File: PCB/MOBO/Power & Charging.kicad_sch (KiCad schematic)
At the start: 53 parts, among them J201 USB_C_Receptacle_PowerOnly_6P, Q1 Si4435DDY, Q2 IRLML6344, Q4 AO3401A, Q5 FS8205A, SW1 SW_DPST_x2, U1 LC709203FQH-01TWG, U2 DW01A, U202 MCP73871-1AA, U205 TPS61230DRC

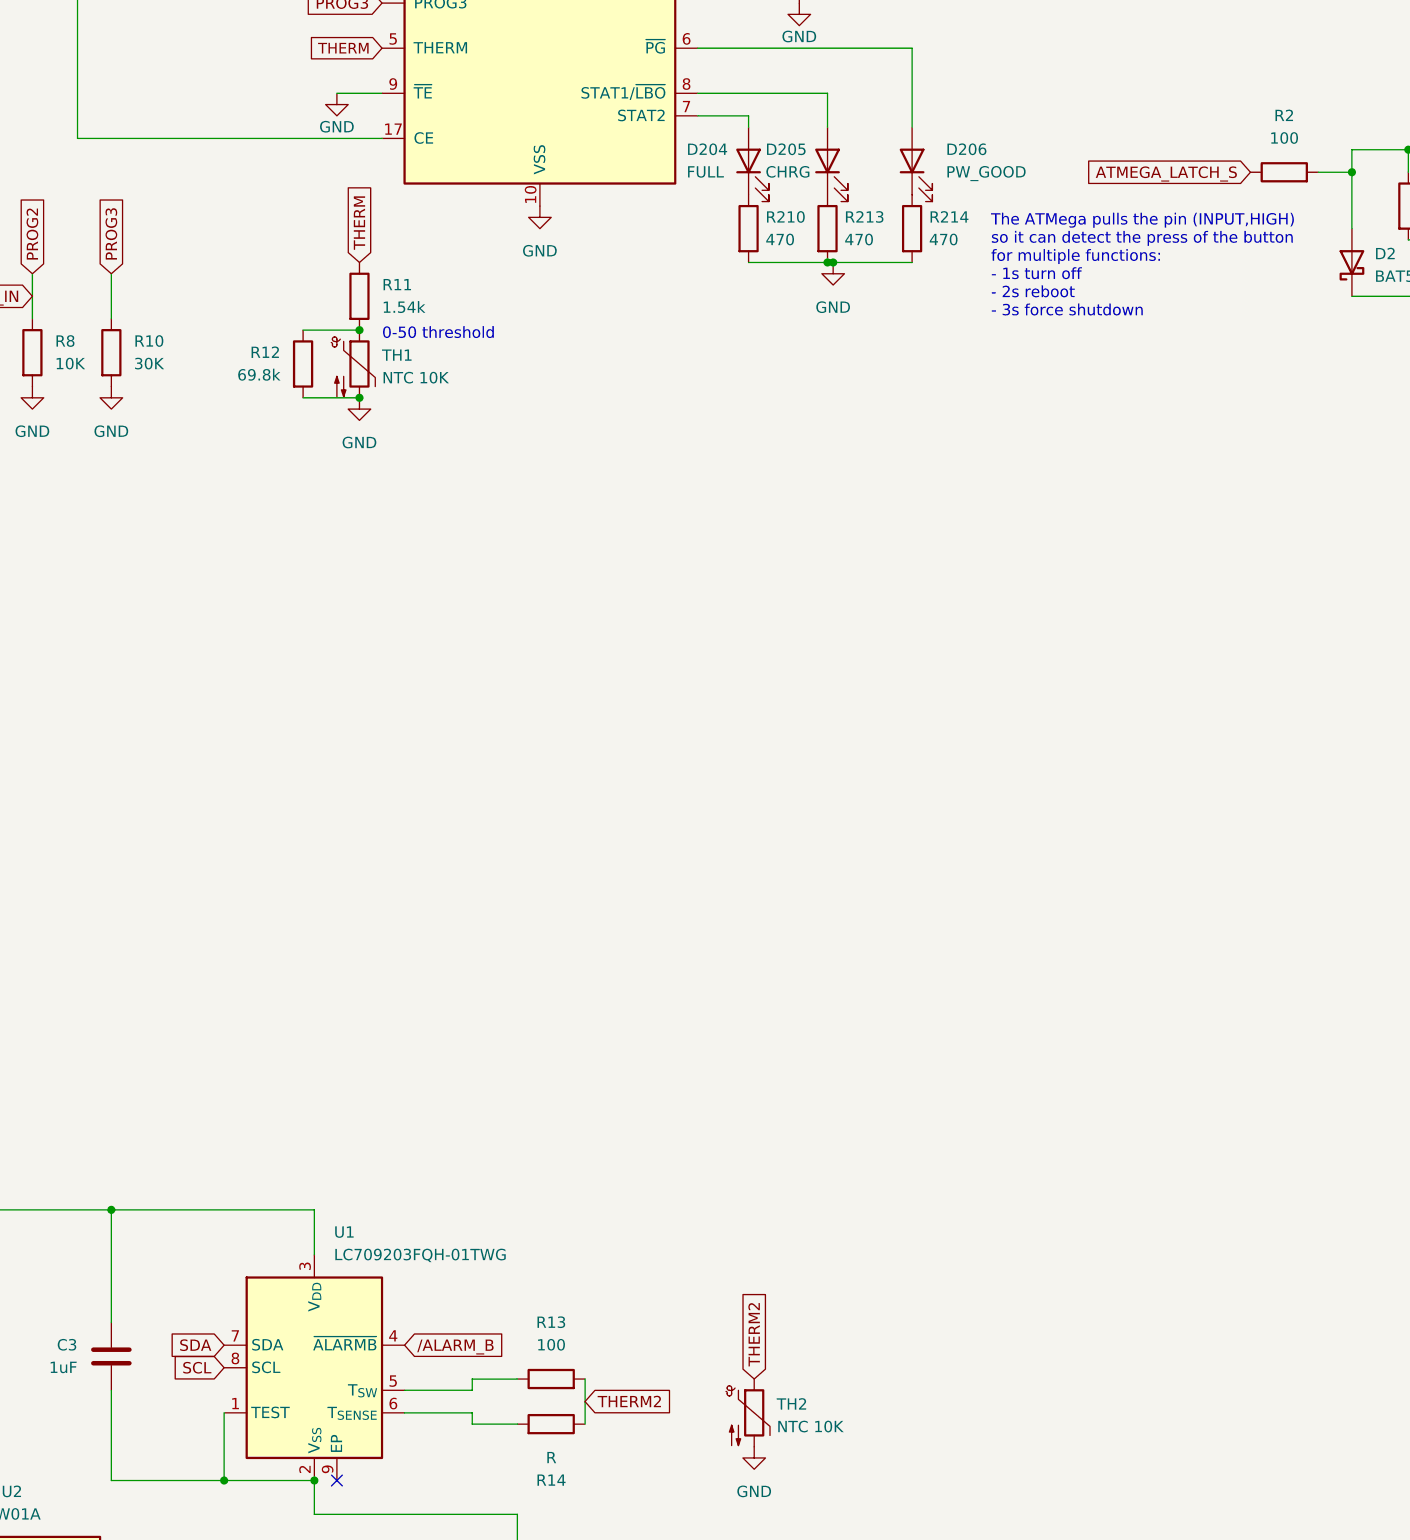
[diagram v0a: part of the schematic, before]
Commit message: fixed sheet conections and added wiring
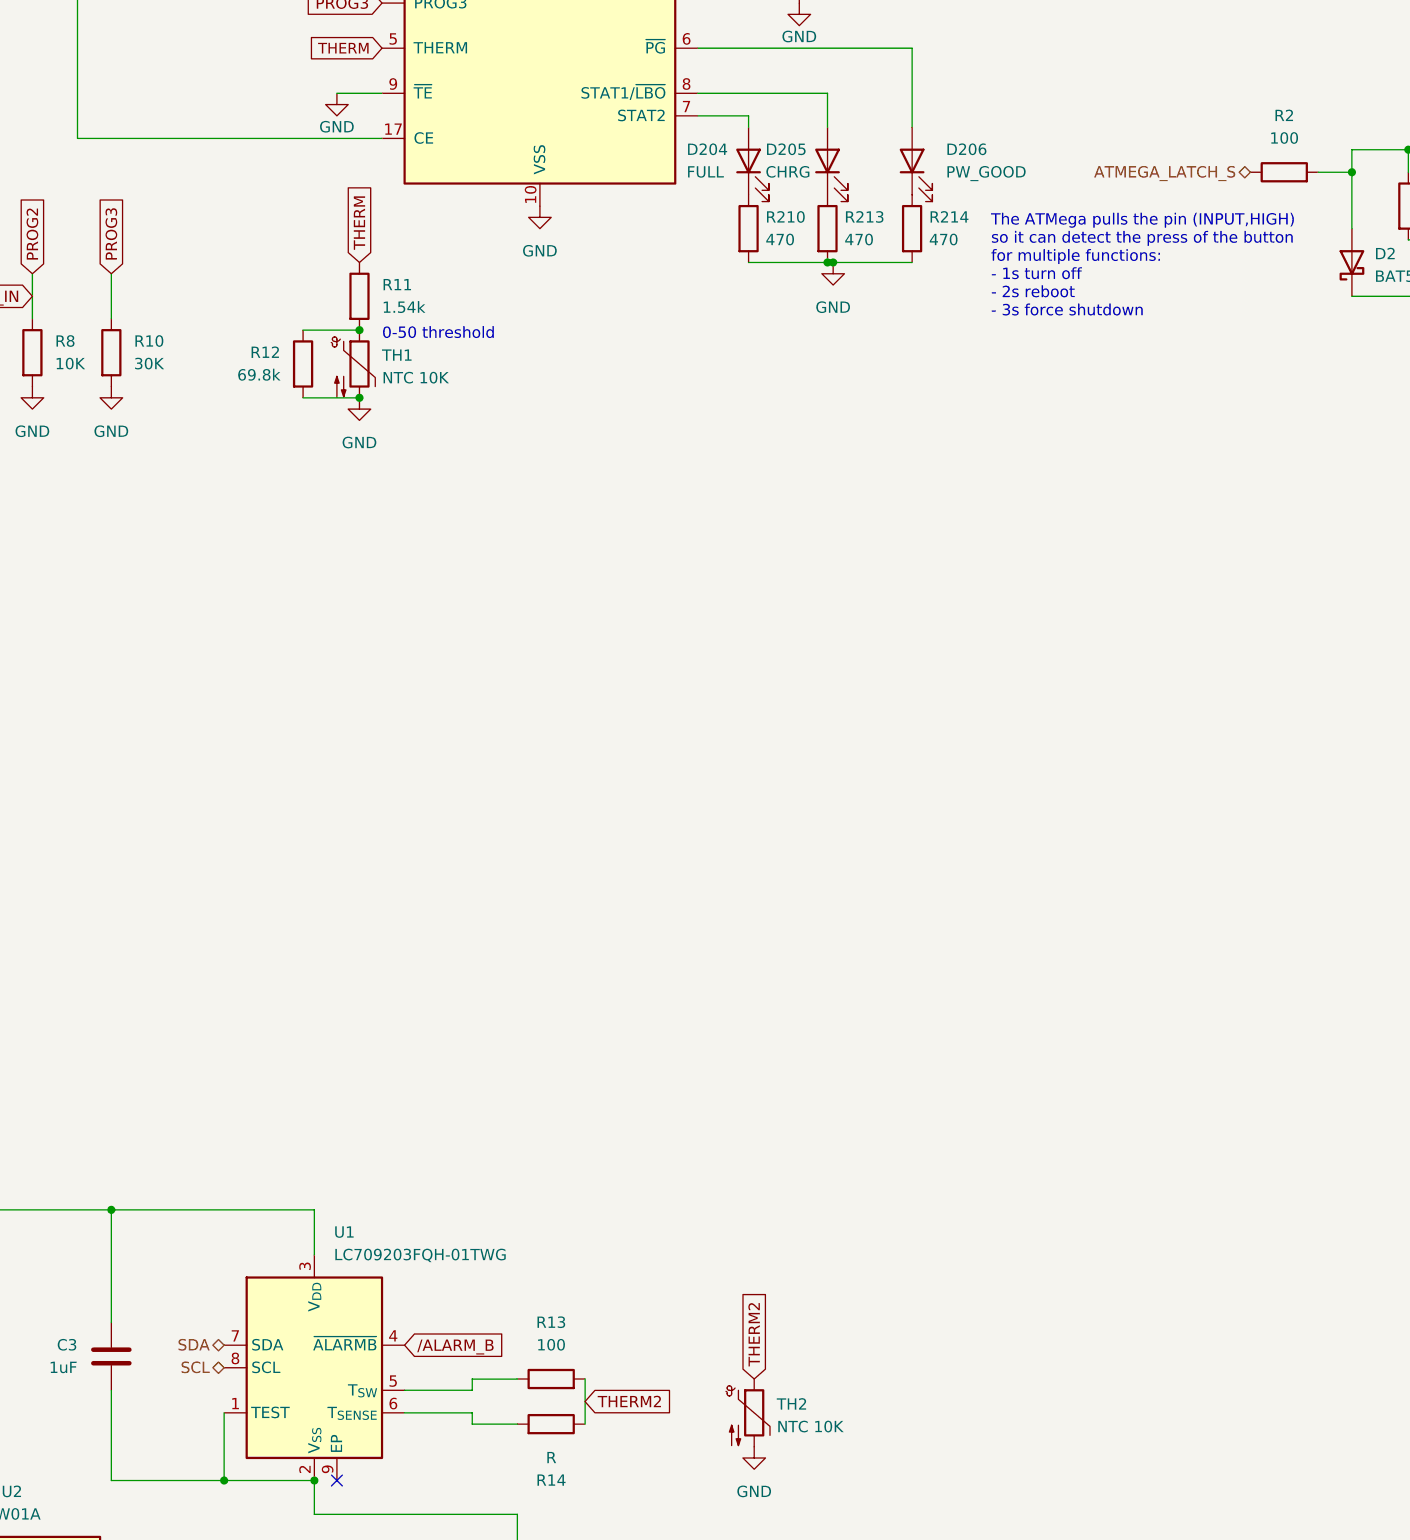
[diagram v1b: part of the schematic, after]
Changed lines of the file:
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@@
-    )
-  )
-  (global_label "SCL" (shape input) (at 119.38 205.74 180) (fields_autoplaced)
-    (effects (font (size 1.27 1.27)) (justify right))
-    (property "Intersheetrefs" "${INTERSHEET_REFS}" (at 112.8872 205.74 0)
-      (effects (font (size 1.27 1.27)) (justify right) hide)
     )
   )
@@
     )
   )
-  (global_label "SDA" (shape input) (at 119.38 203.2 180) (fields_autoplaced)
-    (effects (font (size 1.27 1.27)) (justify right))
-    (property "Intersheetrefs" "${INTERSHEET_REFS}" (at 112.8267 203.2 0)
-      (effects (font (size 1.27 1.27)) (justify right) hide)
-    )
-  )
   (global_label "THERM2" (shape input) (at 179.07 207.01 90) (fields_autoplaced)
     (effects (font (size 1.27 1.27)) (justify left))
@@
     )
   )
-  (global_label "ATMEGA_LATCH_S" (shape input) (at 234.95 71.12 180) (fields_autoplaced)
-    (effects (font (size 1.27 1.27)) (justify right))
-    (property "Intersheetrefs" "${INTERSHEET_REFS}" (at 216.1201 71.12 0)
-      (effects (font (size 1.27 1.27)) (justify right) hide)
-    )
-  )
   (hierarchical_label "3.8V_OUT" (shape input) (at 278.13 36.83 90) (fields_autoplaced)
     (effects (font (size 1.27 1.27)) (justify left))
   )
+  (hierarchical_label "SDA" (shape bidirectional) (at 119.38 203.2 180) (fields_autoplaced)
+    (effects (font (size 1.27 1.27)) (justify right))
+  )
+  (hierarchical_label "SCL" (shape bidirectional) (at 119.38 205.74 180) (fields_autoplaced)
+    (effects (font (size 1.27 1.27)) (justify right))
+  )
+  (hierarchical_label "ATMEGA_LATCH_S" (shape bidirectional) (at 234.95 71.12 180) (fields_autoplaced)
+    (effects (font (size 1.27 1.27)) (justify right))
+  )
   (hierarchical_label "5V_OUT" (shape output) (at 374.65 43.18 0) (fields_autoplaced)

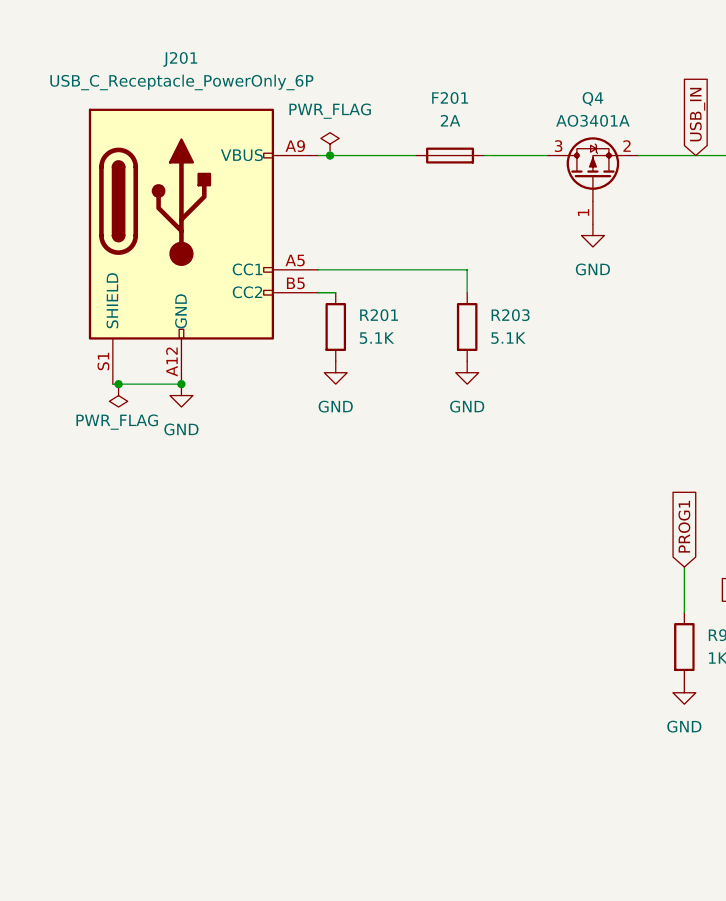
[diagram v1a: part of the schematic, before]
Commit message: relaced usbc port schematic to add data lines
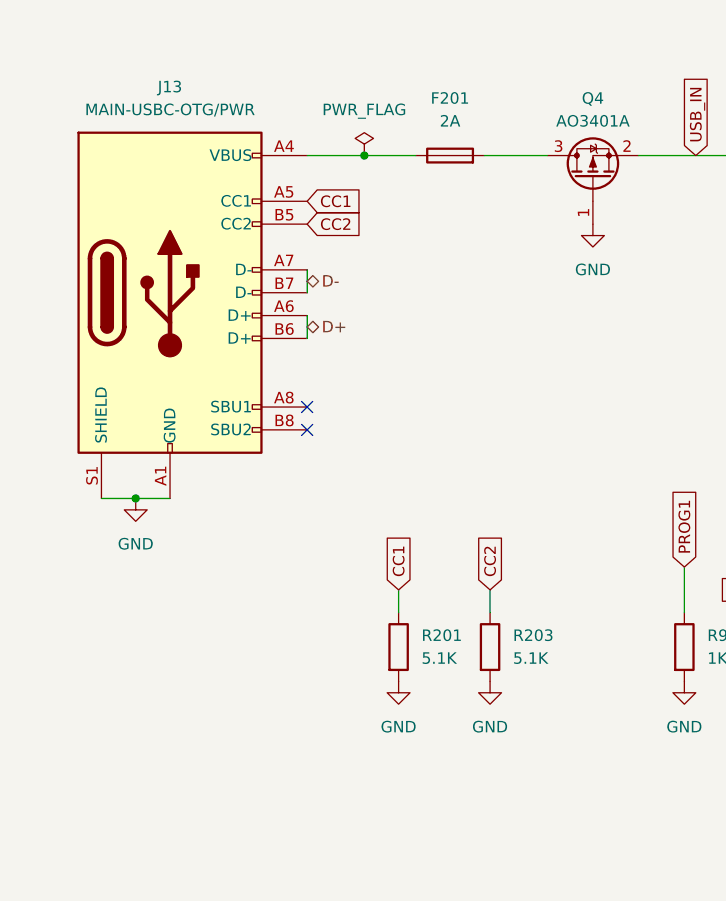
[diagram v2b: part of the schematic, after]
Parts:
- removed J201: USB_C_Receptacle_PowerOnly_6P, Connector_USB:USB_C_Receptacle_Amphenol_12401548E4-2A, symbol Connector:USB_C_Receptacle_PowerOnly_6P
- added J13: MAIN-USBC-OTG/PWR, symbol Connector:USB_C_Receptacle_USB2.0
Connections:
- net GND: now also J13.A1 (GND), J13.A12 (GND), J13.B1 (GND), J13.B12 (GND), J13.S1 (SHIELD)
- net CC2: now reaches R203.1
- net CC2: now also J13.B5 (CC2)
- net at F201.1: now also J13.A4 (VBUS), J13.A9 (VBUS), J13.B4 (VBUS), J13.B9 (VBUS)
- net CC1: now reaches R201.1
- net CC1: now also J13.A5 (CC1)
- new net D+: J13.A6 (D+), J13.B6 (D+)
- new net D-: J13.A7 (D-), J13.B7 (D-)
- no-connect marks 4 -> 6
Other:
- moved on the sheet: R201, R203

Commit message: added connector
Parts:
- renumbered BT1 to BT201, C2 to C201, C203 to C202, C3 to C203, C209 to C204, C210 to C205, C1 to C206, C211 to C207, C212 to C208, C213 to C209, C214 to C210, C215 to C211, D204 to D201, D205 to D202, D206 to D203, D2 to D204, D1 to D205, J13 to J201, L202 to L201, Q4 to Q201, Q5 to Q202, Q2 to Q203, Q1 to Q204, R5 to R202, R9 to R204, R8 to R205, R10 to R206, R4 to R207, R7 to R208, R12 to R209, R11 to R210, R6 to R211, R13 to R212, R14 to R213, R210 to R214, R213 to R215, R214 to R216, R2 to R217, R1 to R218, R3 to R219, R215 to R220, R216 to R221, R217 to R222, SW1 to SW201, TH1 to TH201, TH2 to TH202, U2 to U201, U1 to U202, U202 to U203, U205 to U204

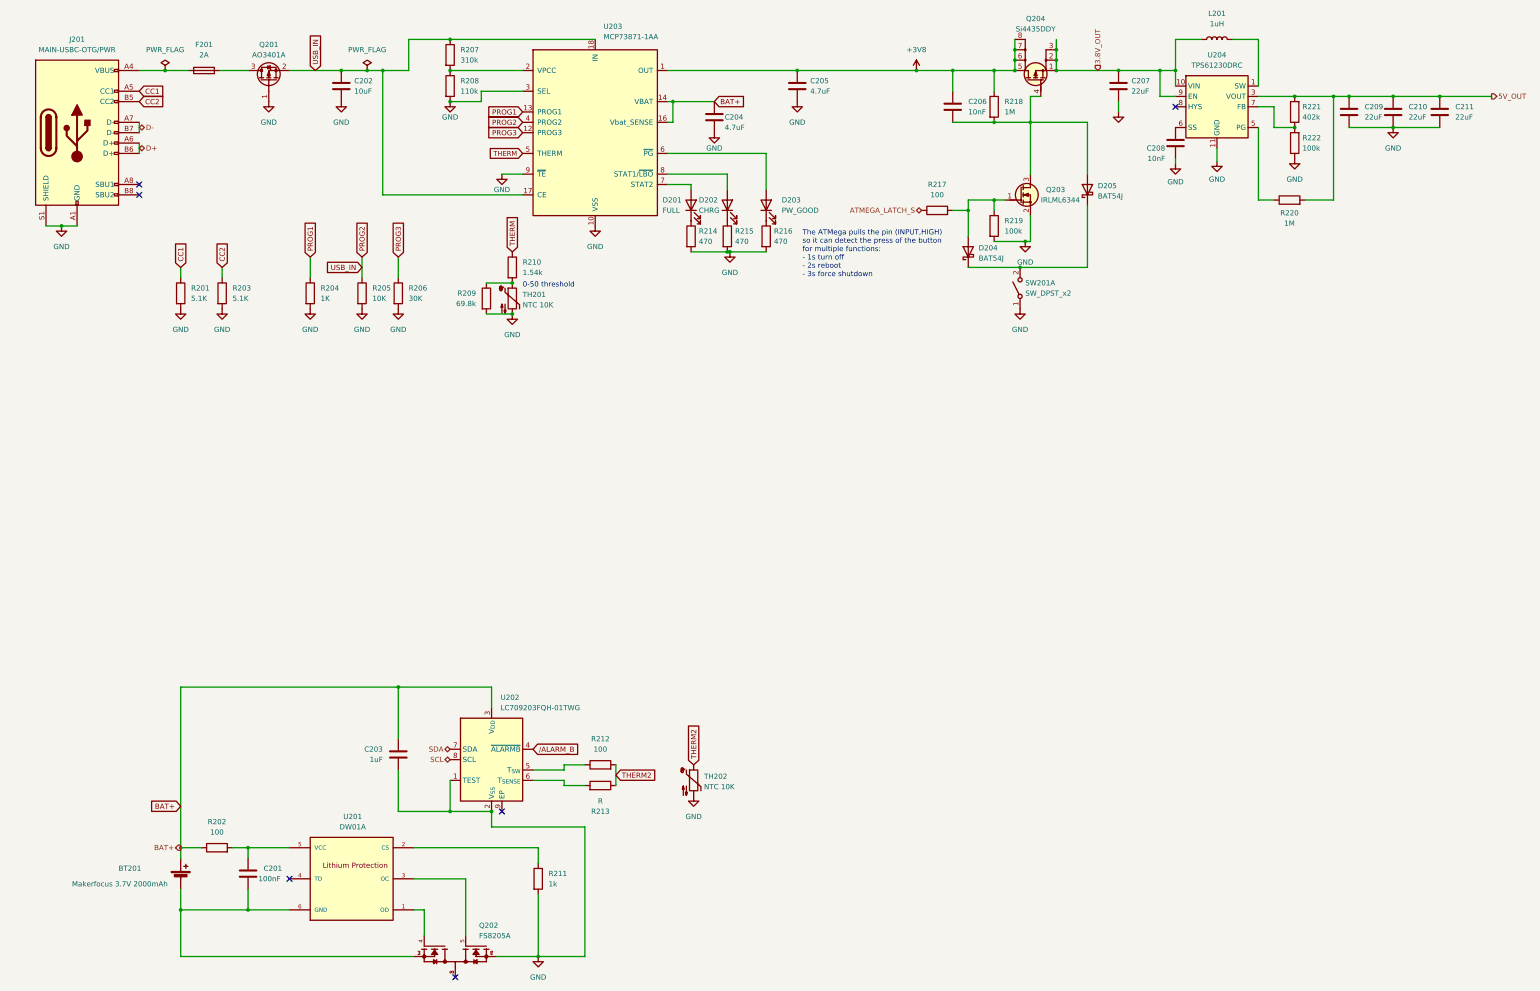
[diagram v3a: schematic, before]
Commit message: schematic cleanup Added:  - Power flags  - Fixed loose connections
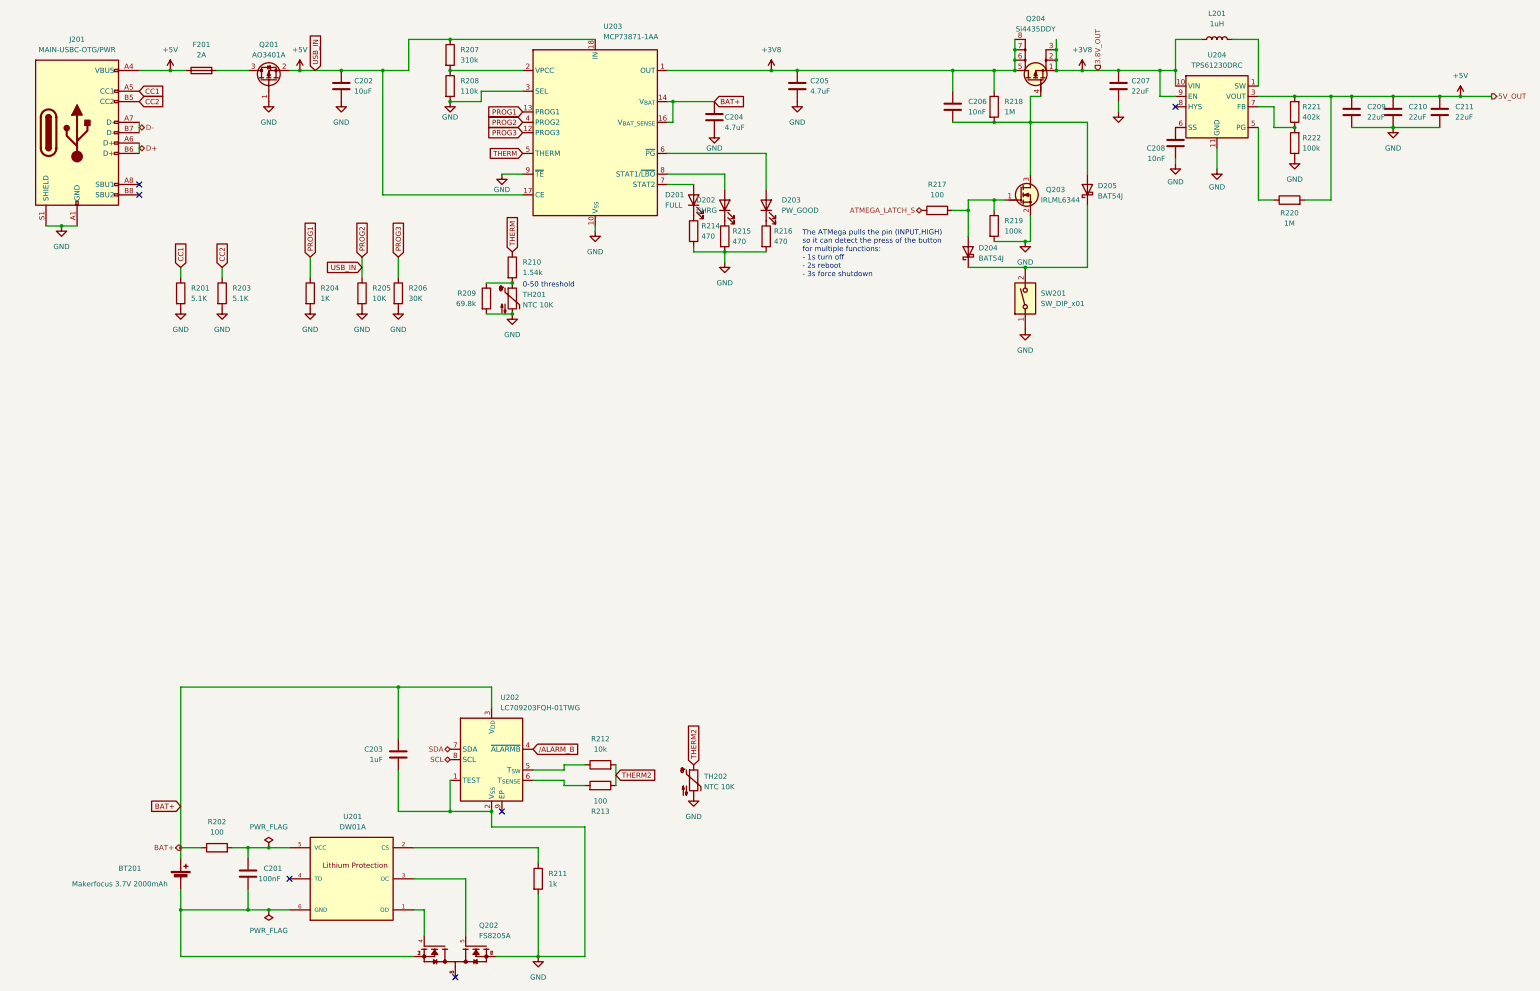
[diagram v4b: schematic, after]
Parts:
- removed SW201: SW_DPST_x2, symbol Switch:SW_DPST_x2
- added SW201: SW_DIP_x01, symbol Switch:SW_DIP_x01
- R212: value 100 -> 10k
- R213: value R -> 100
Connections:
- net 3.8V_OUT is gone; now on net +3V8: C207.1, L201.1, Q204.1 (S), Q204.2 (S), Q204.3 (S), U204.10 (VIN), U204.9 (EN)
- net 5V_OUT is gone; now on net +5V: C209.1, C210.1, C211.1, R220.2, R221.2, U204.3 (VOUT), U204.4 (VOUT)
- net PROG2 is gone; now on net +5V: C202.1, Q201.2 (S), R205.1, R207.1, U203.17 (CE), U203.18 (IN), U203.19 (IN), U203.4 (PROG2)
- net GND: now also SW201.1
- net at D204.1 (K), D205.1 (K): now also SW201.2
- net +5V: now reaches F201.1, J201.A4 (VBUS), J201.A9 (VBUS), J201.B4 (VBUS), J201.B9 (VBUS)
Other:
- moved on the sheet: C209, D201, D202, F201, R214, R215
